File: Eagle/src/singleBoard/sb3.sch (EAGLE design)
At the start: 51 parts, among them U1 GY-521MPU6050

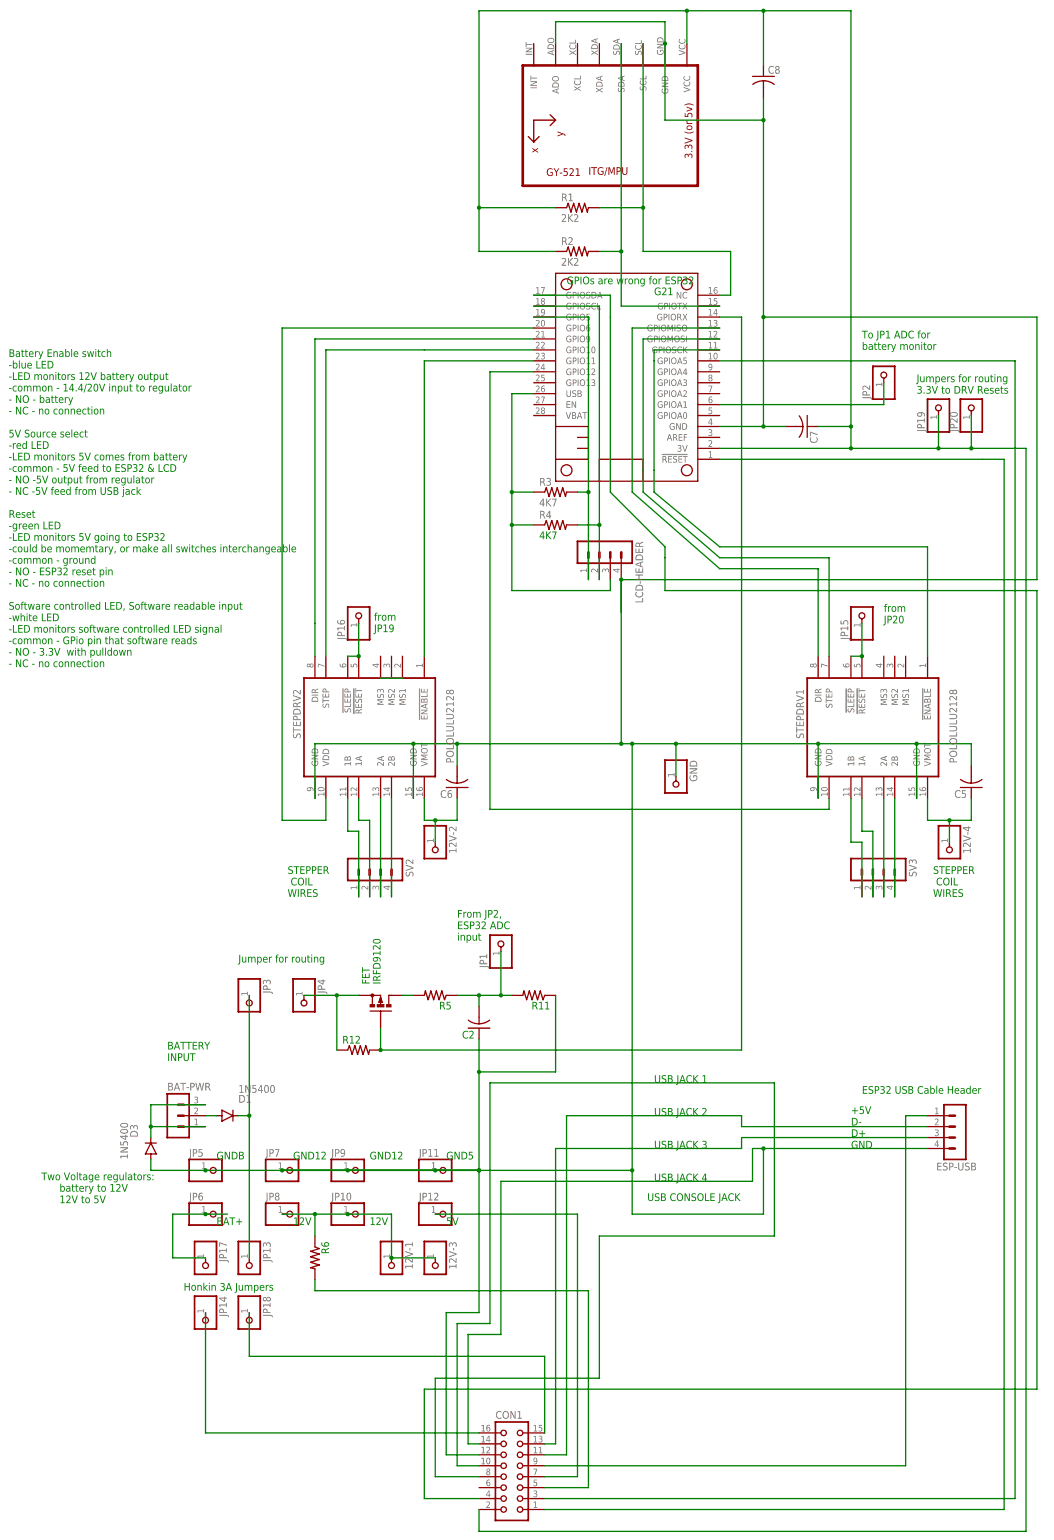
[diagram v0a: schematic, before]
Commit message: minor fixes before release to manufacturing
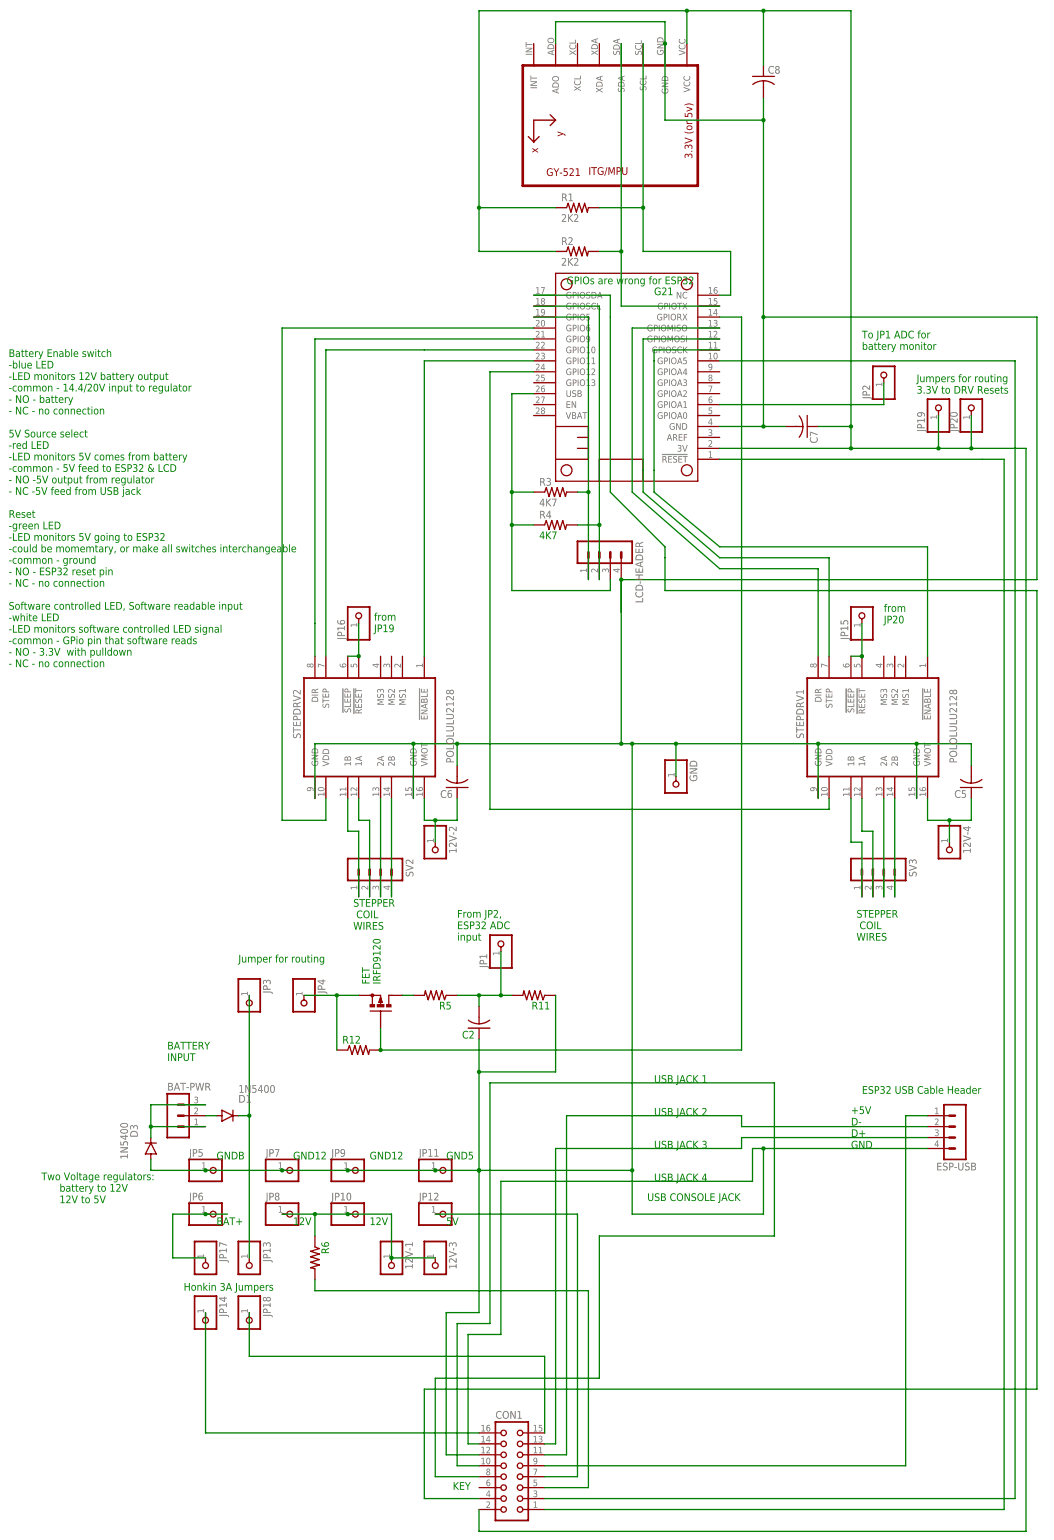
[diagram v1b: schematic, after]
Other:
- note added: "KEY"
